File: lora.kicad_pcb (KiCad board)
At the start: 2 copper layers, 55 parts, among them J1 Conn_01x02, J10 Conn, J11 Conn_Coaxial, J2 Humidity, J3 Temp, J4 Programming_Jumper, J5 Temp, J6 VDD, J7 GPS, J8 SIM800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

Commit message: some more structure and 2 additonal layers, first board outlines....
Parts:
- U3: moved to B.Cu
- moved J10 236.1 mm to (269.0, 114.0)
- moved J2 207.8 mm to (222.0, 130.0)
- moved J3 202.9 mm to (226.0, 130.0)
- moved J8 195.2 mm to (222.0, 117.5)
- moved Q1 188.2 mm to (217.8, 129.8)
- moved R1 185.9 mm to (215.0, 130.2), turned to 90 degrees
- moved R2 181.2 mm to (214.8, 127.0)
- moved SW2 165.8 mm to (198.0, 75.0)
- moved J5 164.6 mm to (172.0, 133.0), turned to 180 degrees
- moved J9 151.2 mm to (172.0, 116.4)
- moved Q5 129.1 mm to (231.0, 154.9)
- moved R19 129.1 mm to (225.3, 153.6)
- moved J7 127.0 mm to (115.0, 141.4)
- moved J1 118.9 mm to (152.0, 97.0)
- moved D2 116.8 mm to (161.2, 95.5)
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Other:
- board outline added: 80 x 45 mm
- copper layers 2 -> 4
- board text added: "PCB Antenna Design here!"

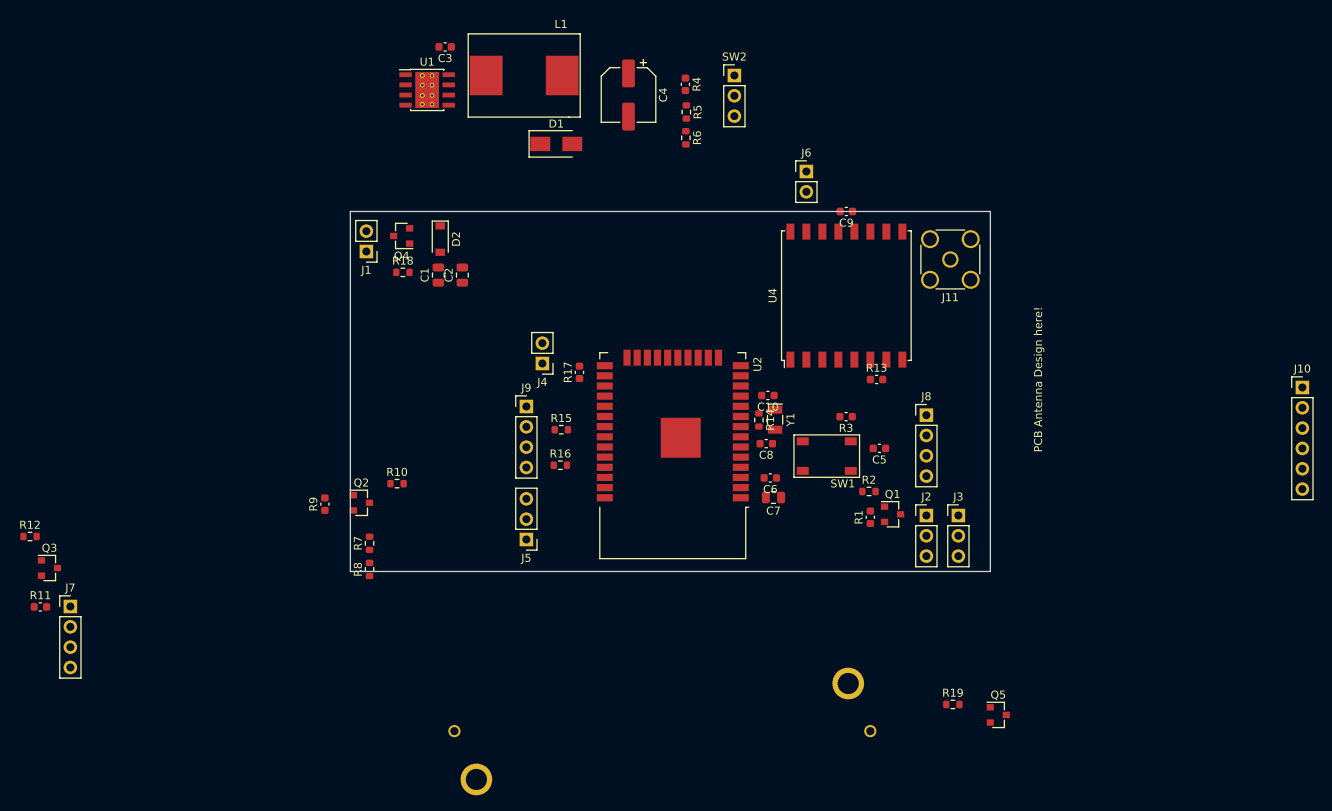
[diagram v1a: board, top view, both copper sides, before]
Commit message: some progress with layout. Added ferrit bead to schematic.
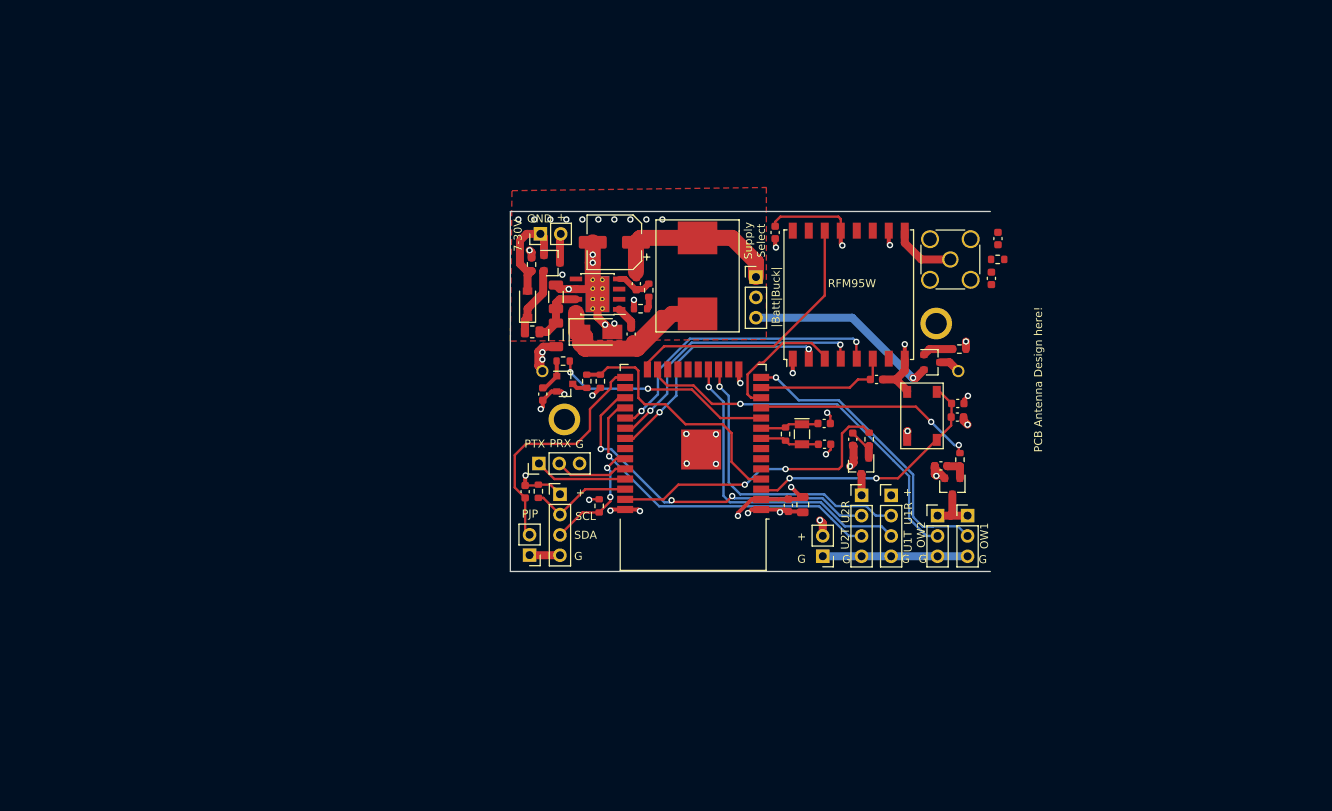
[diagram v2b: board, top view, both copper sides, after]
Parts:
- removed J10: Conn, Connector_PinHeader_2.54mm:PinHeader_1x06_P2.54mm_Vertical
- added C11: dnp, Capacitor_SMD:C_0603_1608Metric, F.Cu at (230.1, 100.4)
- added C12: dnp, Capacitor_SMD:C_0603_1608Metric, F.Cu at (230.9, 95.4)
- added FB1: Ferrite_Bead_Small, Resistor_SMD:R_0805_2012Metric, F.Cu at (172.7, 107.0)
- added L2: 0R, Resistor_SMD:R_0603_1608Metric, F.Cu at (230.9, 98.0)
- C1, C2: footprint Capacitor_SMD:C_0805_2012Metric -> Capacitor_SMD:C_1206_3216Metric
- R7: value 3k -> 30k
- R8: value 1k -> 10k
- moved R12 105.6 mm to (214.8, 120.5), turned to 270 degrees
- moved R11 103.7 mm to (212.8, 120.5), turned to 90 degrees
- moved Q3 102.3 mm to (213.8, 123.8), turned to 270 degrees
- moved J7 99.9 mm to (213.9, 127.5)
- moved J6 48.1 mm to (209.1, 135.1), turned to 180 degrees
- moved U3 46.3 mm to (200.0, 112.0)
- moved Q5 44.9 mm to (222.7, 110.8)
- moved R19 44.4 mm to (226.1, 109.2)
- moved C3 42.8 mm to (185.1, 107.3), turned to 90 degrees
- moved R8 37.2 mm to (181.2, 113.2)
- moved R7 33.9 mm to (179.6, 113.2), turned to 270 degrees
- moved U1 33.2 mm to (180.9, 102.3), turned to 180 degrees
- moved L1 33.1 mm to (193.4, 100.0), turned to 270 degrees
- moved R9 30.5 mm to (174.1, 114.8)
- moved Q2 29.4 mm to (176.8, 113.5)
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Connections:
- D2 pad 1: VSUPPLY -> Net-(D2-Pad1)
- Q4 pad 2: VSUPPLY -> Net-(D2-Pad1)
- U2 pad 16: IO13 -> Net-(U2-Pad16)
- U2 pad 26: IO4 -> Net-(U2-Pad26)
- U2 pad 5: SENSOR_VN -> Net-(U2-Pad5)
- U2 pad 6: IO34 -> Net-(U2-Pad6)
- U2 pad 7: IO35 -> Net-(U2-Pad7)
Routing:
- net GND: track 0.00 -> 91.1 mm, vias 0 -> 39
- net ONEWIRE2_DATA: track 0.00 -> 47.0 mm, vias 0 -> 1
- net VDD: track 0.00 -> 46.4 mm, vias 0 -> 11
- net UART2_RX: track 0.00 -> 45.0 mm, vias 0 -> 3
- net Net-(C3-Pad1): track 0.00 -> 43.9 mm
- net UART2_TX: track 0.00 -> 43.1 mm, vias 0 -> 1
- net UART1_TX: track 0.00 -> 39.6 mm, vias 0 -> 1
- net SPI_CS: track 0.00 -> 37.9 mm, vias 0 -> 2
- net ONEWIRE1_DATA: track 0.00 -> 37.1 mm, vias 0 -> 1
- net GPS_MOSFET_SWITCH: track 0.00 -> 36.9 mm, vias 0 -> 2
- net UART1_RX: track 0.00 -> 36.7 mm, vias 0 -> 1
- net SPI_SCK: track 0.00 -> 36.0 mm, vias 0 -> 2
- net RFM_DIO0: track 0.00 -> 34.6 mm
- net SPI_MISO: track 0.00 -> 32.5 mm, vias 0 -> 2
- net RESET: track 0.00 -> 32.4 mm, vias 0 -> 2
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- added copper zone on F.Cu, net GND
- added copper zone on In1.Cu_GND, net GND
- added copper zone on In2.Cu_VDD, net VDD
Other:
- board size 80 x 45 mm -> 60 x 45 mm
- net class Default: via_drill 0.4 -> 0.45
- board text added: "+"
- board text added: "7-30V"
- board text added: "G"
- board text added: "GND"
- board text added: "OW1"
- board text added: "OW2"
- board text added: "PJP"
- board text added: "PRX"
- board text added: "PTX"
- board text added: "RFM95W"
- board text added: "SCL"
- board text added: "SDA"
- board text added: "Supply Select"
- board text added: "U1R"
- board text added: "U1T"
- board text added: "U2R"
- board text added: "U2T"
- board text added: "|Batt|Buck|"

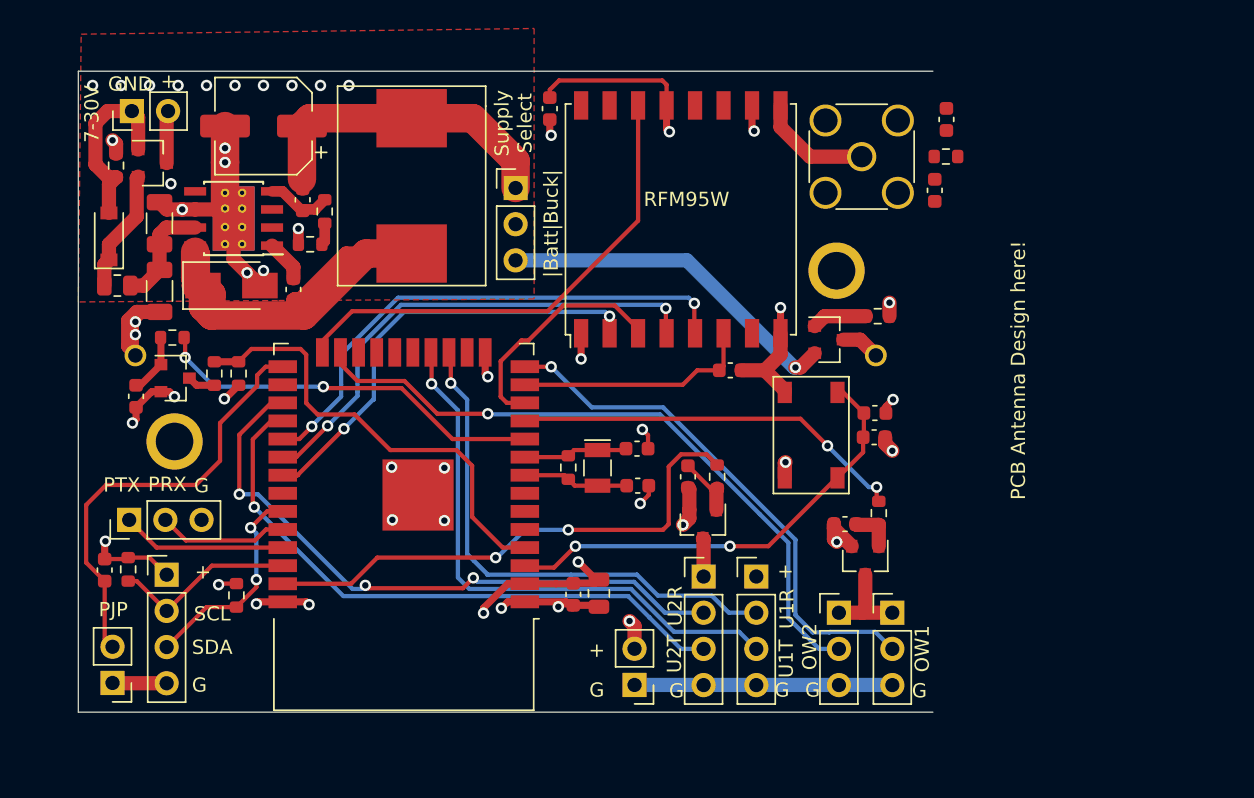
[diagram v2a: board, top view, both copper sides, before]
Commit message: added cutouts for antenna.
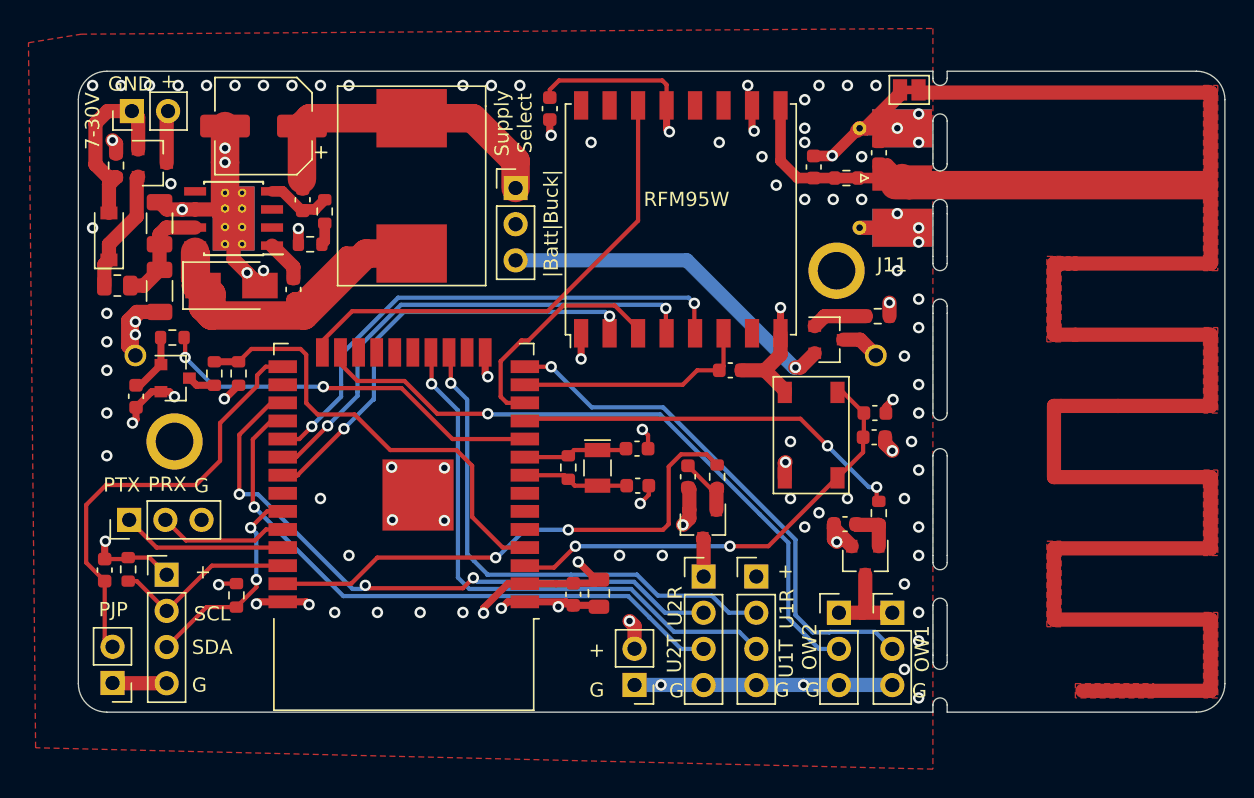
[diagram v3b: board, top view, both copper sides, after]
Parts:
- added JP1: SolderJumper_2_Bridged, Jumper:SolderJumper-2_P1.3mm_Bridged_Pad1.0x1.5mm, F.Cu at (228.3, 93.3)
- J11: footprint Connector_Coaxial:SMA_Amphenol_132134_Vertical -> Connector_Coaxial:SMA_Molex_73251-2120_EdgeMount_Horizontal
- L2: value 0R -> dnp
- U3: footprint 2460 -> SamacSys_Parts:2460
- moved C11 8.66 mm to (221.6, 98.7), turned to 270 degrees
- moved L2 7.15 mm to (223.9, 99.5)
- moved C12 5.29 mm to (226.2, 97.7)
- moved J11 3.21 mm to (227.8, 99.5), turned to 0 degrees
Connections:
- C12 pad 2: Net-(C12-Pad2) -> Net-(C11-Pad2)
- L2 pad 2: Net-(C12-Pad2) -> Net-(C11-Pad2)
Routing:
- net Net-(C11-Pad2): track 8.09 -> 175.4 mm
- net GND: track 91.1 -> 111.4 mm, vias 39 -> 101
- added copper zone on F.Cu, net Net-(C11-Pad2)
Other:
- board size 60 x 45 mm -> 80.5 x 45 mm
- board text removed: "PCB Antenna Design here!"

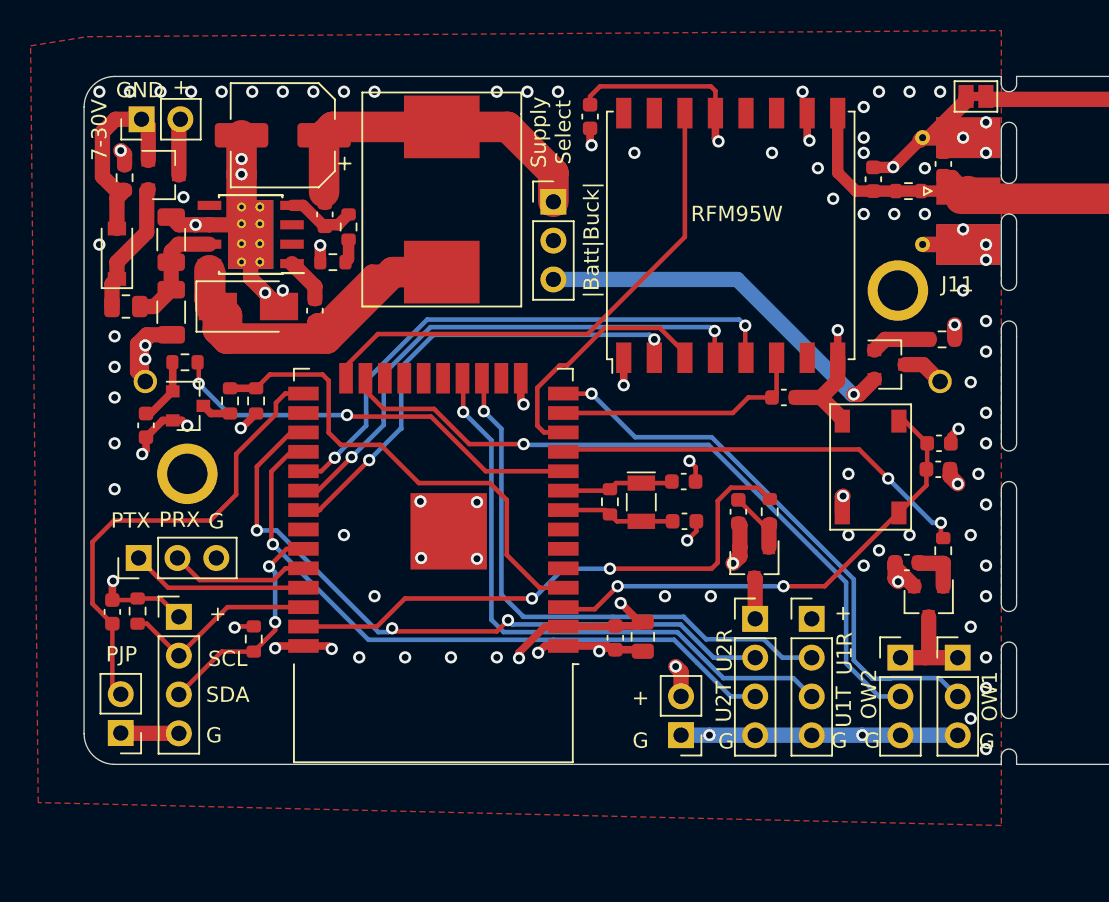
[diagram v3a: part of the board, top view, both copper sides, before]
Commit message: added mounting holes for GPS
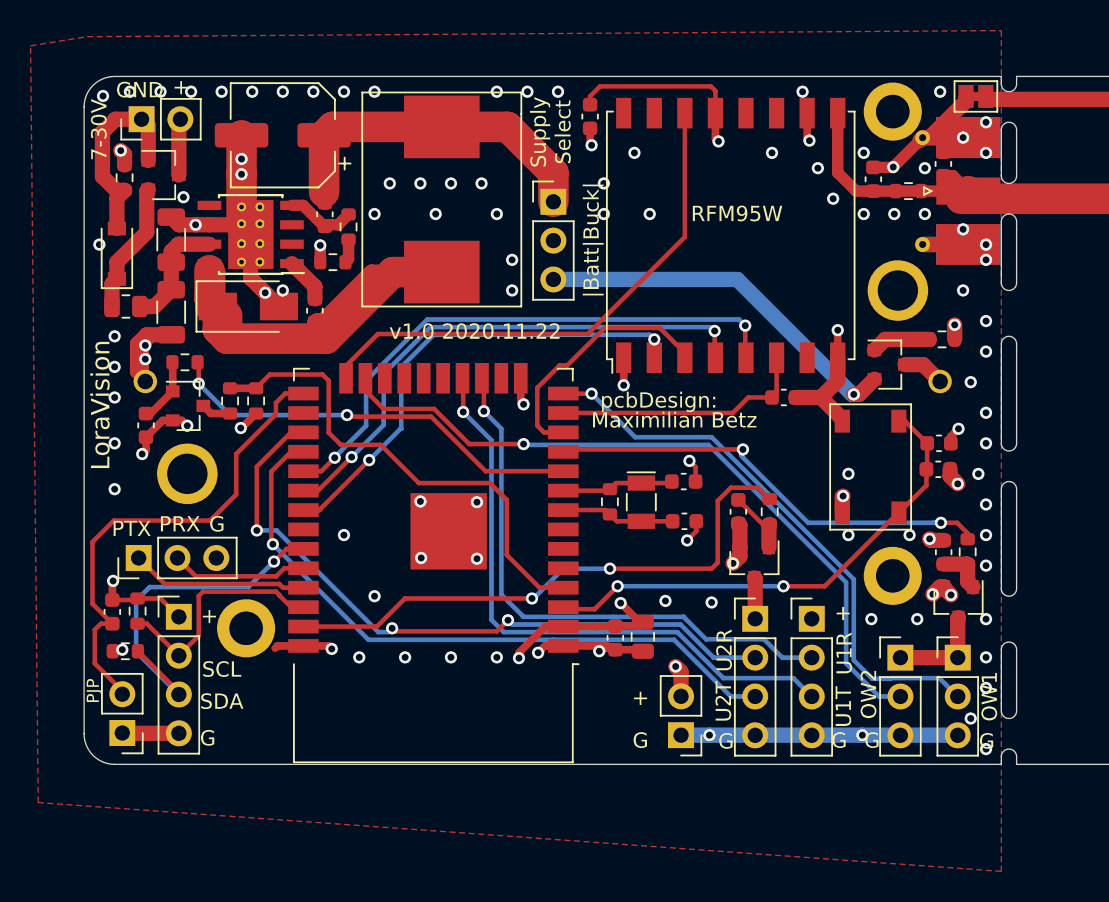
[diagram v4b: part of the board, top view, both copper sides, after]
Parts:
- added H1: MountingHole_Pad, MountingHole:MountingHole_2.2mm_M2_DIN965_Pad, F.Cu at (222.9, 94.3)
- added H2: MountingHole_Pad, MountingHole:MountingHole_2.2mm_M2_DIN965_Pad, F.Cu at (180.6, 128.1)
- added H3: MountingHole_Pad, MountingHole:MountingHole_2.2mm_M2_DIN965_Pad, F.Cu at (222.9, 124.7)
- moved R15 8.44 mm to (172.7, 129.6), turned to 0 degrees
- moved R1 2.50 mm to (226.2, 123.1), turned to 270 degrees
- moved Q1 1.95 mm to (227.2, 126.4)
- moved R2 1.60 mm to (227.8, 123.1)
- moved J4 0.10 mm to (172.5, 134.9)
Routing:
- net I2C_SDA: track 15.9 -> 24.4 mm, vias 2 -> 1
- net VDD_SENSOR_MOSFET_SWITCH: track 27.8 -> 30.3 mm
- net I2C_SCL: track 13.0 -> 15.4 mm
- net PRG_JP: track 30.6 -> 32.0 mm
- net VDD: track 46.4 -> 45.0 mm, vias 11 -> 13
- net GND: vias 101 -> 107
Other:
- outline, holes or cut-outs redrawn
- board text added: "LoraVision"
- board text added: "Maximilian Betz"
- board text added: "pcbDesign:"
- board text added: "v1.0 2020.11.22"

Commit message: plotted first gerber files.
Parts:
- moved H1 0.20 mm to (222.7, 94.3)
- moved H3 0.20 mm to (222.7, 124.7)
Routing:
- net GND: vias 107 -> 109
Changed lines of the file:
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@@
     (thickness 1.6)
     (drawings 75)
-    (tracks 644)
+    (tracks 646)
     (zones 0)
     (modules 62)
@@
   (layers
     (0 F.Cu signal)
-    (1 In1.Cu_GND power hide)
-    (2 In2.Cu_VDD power hide)
+    (1 In1.Cu_GND power)
+    (2 In2.Cu_VDD power)
     (31 B.Cu signal)
     (32 B.Adhes user)
@@
   )
   (module MountingHole:MountingHole_2.2mm_M2_DIN965_Pad (layer F.Cu)
-    (at 222.9 94.3)
+    (at 222.7 94.3)
     (descr "Mounting Hole 2.2mm, M2, DIN965")
     (tags "mounting hole 2.2mm m2 din965")
@@
   )
   (module MountingHole:MountingHole_2.2mm_M2_DIN965_Pad (layer F.Cu)
-    (at 222.9 124.67)
+    (at 222.7 124.67)
     (descr "Mounting Hole 2.2mm, M2, DIN965")
     (tags "mounting hole 2.2mm m2 din965")
@@
     (effects (font (size 1 1) (thickness 0.15)))
   )
-  (gr_text LoraVision (at 171.1 113.5 90) (layer F.SilkS)
+  (gr_text LoraVision (at 171.5 113.5 90) (layer F.SilkS)
     (effects (font (size 1.2 1.2) (thickness 0.2)))
   )
-  (gr_text "v1.0 2020.11.22" (at 195.6 108.7) (layer F.SilkS)
+  (gr_text "v1.0 2020.11.22" (at 193 108.7) (layer F.SilkS)
     (effects (font (size 1 1) (thickness 0.15)))
   )
-  (gr_text "Maximilian Betz" (at 208.6 114.5) (layer F.SilkS)
+  (gr_text "Maximilian Betz" (at 209.93 114.97) (layer F.SilkS)
     (effects (font (size 1 1) (thickness 0.2)))
   )
-  (gr_text pcbDesign: (at 207.6 113.2) (layer F.SilkS)
+  (gr_text pcbDesign: (at 207.97 113.37) (layer F.SilkS)
     (effects (font (size 1 1) (thickness 0.15)))
   )
@@
   (segment (start 210.91 135.09) (end 220.91 135.09) (width 1) (layer B.Cu) (net 2))
   (via (at 210.91 135.09) (size 0.8) (drill 0.45) (layers F.Cu B.Cu) (net 2))
-  (via (at 172 119) (size 0.8) (drill 0.45) (layers F.Cu B.Cu) (net 2))
-  (via (at 172 116) (size 0.8) (drill 0.45) (layers F.Cu B.Cu) (net 2))
-  (via (at 172 113) (size 0.8) (drill 0.45) (layers F.Cu B.Cu) (net 2))
-  (via (at 172 111) (size 0.8) (drill 0.45) (layers F.Cu B.Cu) (net 2))
-  (via (at 172 109) (size 0.8) (drill 0.45) (layers F.Cu B.Cu) (net 2))
+  (via (at 172.5 118) (size 0.8) (drill 0.45) (layers F.Cu B.Cu) (net 2))
+  (via (at 172.5 115.5) (size 0.8) (drill 0.45) (layers F.Cu B.Cu) (net 2))
+  (via (at 172.5 113) (size 0.8) (drill 0.45) (layers F.Cu B.Cu) (net 2))
+  (via (at 172.5 111) (size 0.8) (drill 0.45) (layers F.Cu B.Cu) (net 2))
+  (via (at 172.5 109) (size 0.8) (drill 0.45) (layers F.Cu B.Cu) (net 2))
   (via (at 171 103) (size 0.8) (drill 0.45) (layers F.Cu B.Cu) (net 2))
   (via (at 197 93) (size 0.8) (drill 0.45) (layers F.Cu B.Cu) (net 2))
@@
   (via (at 224.5 127.5) (size 0.8) (drill 0.45) (layers F.Cu B.Cu) (net 2))
   (via (at 221.5 127.5) (size 0.8) (drill 0.45) (layers F.Cu B.Cu) (net 2))
+  (via (at 172.5 120) (size 0.8) (drill 0.45) (layers F.Cu B.Cu) (net 2))
+  (via (at 223 103) (size 0.8) (drill 0.45) (layers F.Cu B.Cu) (net 2))
   (segment (start 185.1 105.745) (end 183.6 104.245) (width 1) (layer F.Cu) (net 3))
   (segment (start 185.1 106.55) (end 185.1 105.745) (width 1) (layer F.Cu) (net 3))

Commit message: schönen Lattenzaun! added Toolingholes, and JLCPCB number location.
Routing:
- net GND: track 111.4 -> 135.2 mm, vias 109 -> 136
- net SPI_SCK: track 36.0 -> 34.0 mm
- net SPI_MISO: track 32.5 -> 30.7 mm
- net SPI_CS: track 37.9 -> 36.3 mm
- net Net-(C3-Pad1): track 43.9 -> 45.0 mm
- net Net-(C11-Pad2): track 175.4 -> 174.8 mm
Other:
- outline, holes or cut-outs redrawn
- board text added: "JLCJLCJLCJLC"
- board text removed: "GND"
